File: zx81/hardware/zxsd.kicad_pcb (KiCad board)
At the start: 2 copper layers, 69.9 x 95.9 mm, 37 parts, among them J1 Micro_SD_Card, J2 ZX81_EXP, SW1 RESET, U1 74HCT32, U10 27C256, U11 KM62256CLP, U2 74HCT32, U3 74HCT00, U4 74HCT02, U5 74HCT163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

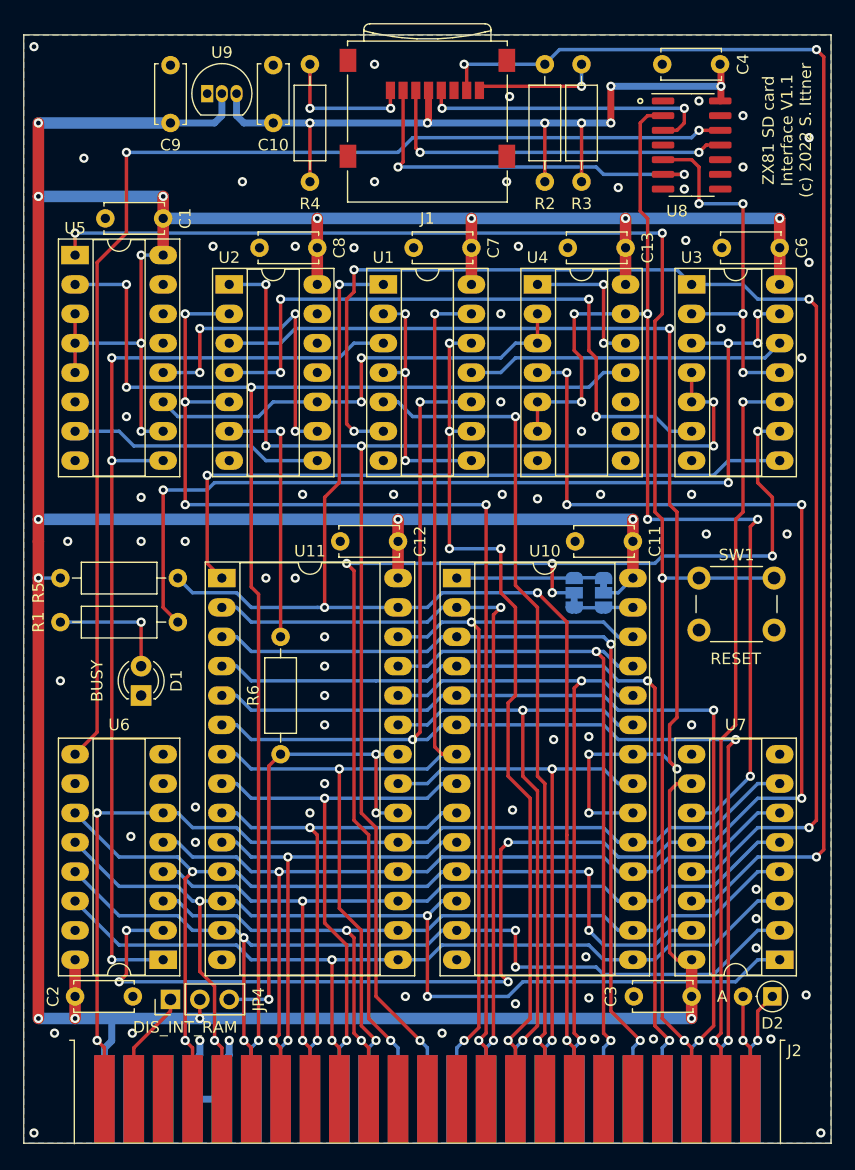
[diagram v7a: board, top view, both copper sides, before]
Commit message: fixed HRG issue, consider nRFSH for memory decoding
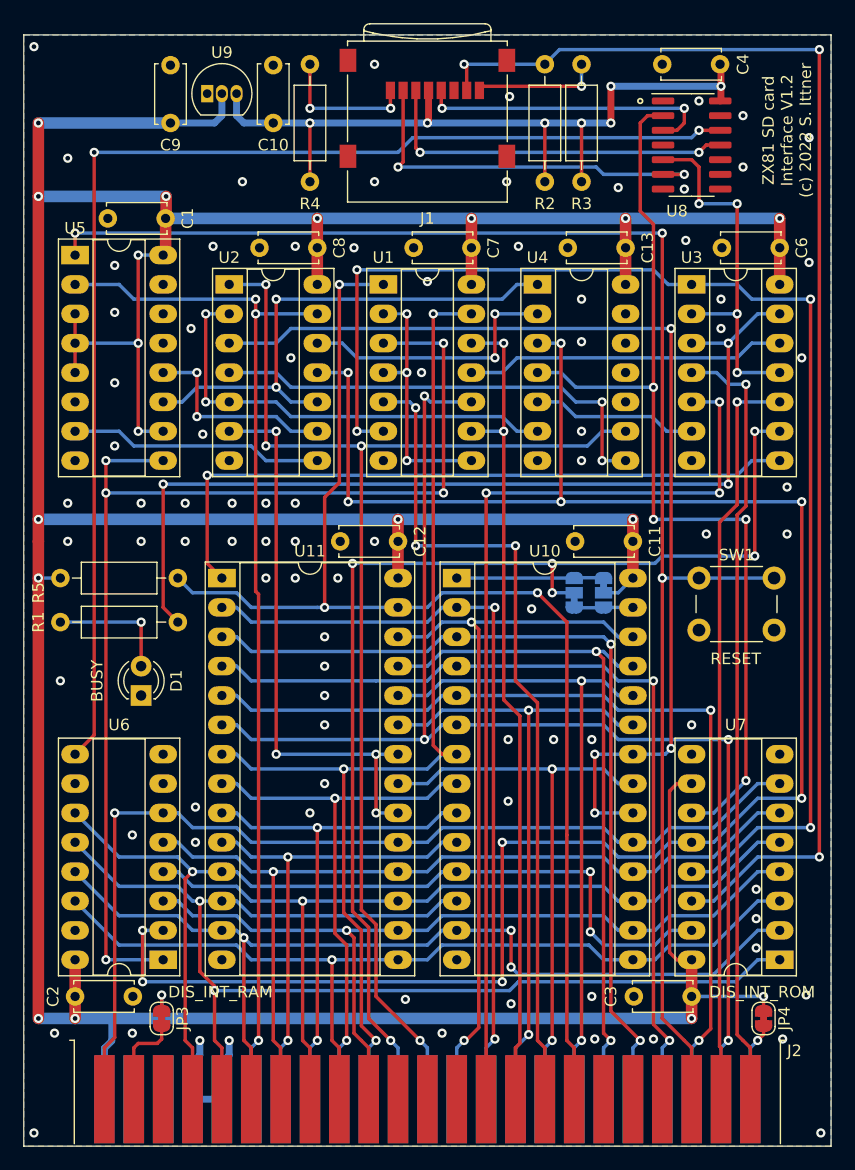
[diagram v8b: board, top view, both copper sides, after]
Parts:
- removed D2: BAT43, Diode_THT:D_DO-35_SOD27_P2.54mm_Vertical_AnodeUp
- removed R6: 680R, Resistor_THT:R_Axial_DIN0207_L6.3mm_D2.5mm_P10.16mm_Horizontal
- added JP3: DIS_INT_RAM, Jumper:SolderJumper-2_P1.3mm_Bridged_RoundedPad1.0x1.5mm, F.Cu at (124.3, 128.3)
- JP4: value DIS_INT_RAM -> DIS_INT_ROM; footprint Connector_PinHeader_2.54mm:PinHeader_1x03_P2.54mm_Vertical -> Jumper:SolderJumper-2_P1.3mm_Bridged_RoundedPad1.0x1.5mm
- U4: value 74HCT02 -> 74HCT04
- moved JP4 51.3 mm to (176.4, 128.3), turned to -90 degrees
- moved C1 0.21 mm to (124.7, 59.1)
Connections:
- JP4 pad 1: /nRAMCS_INT -> +5V
- JP4 pad 2: +5V -> /nROMCS_INT
- U2 pad 11: unconnected-(U2-Pad11) -> /nSD_CLK
- U2 pad 12: GND -> Net-(U2-Pad12)
- U2 pad 13: GND -> /CLK
- U2 pad 2: /nMREQ -> Net-(U2-Pad2)
- U2 pad 5: /nMREQ -> Net-(U2-Pad2)
- U2 pad 6: Net-(R6-Pad2) -> /nCS_RAM
- U3 pad 4: /A14 -> /nRFSH
- U3 pad 5: /A14 -> /nMREQ
- U3 pad 6: Net-(U2-Pad4) -> Net-(U3-Pad6)
- U4 pad 1: Net-(U4-Pad1) -> Net-(U2-Pad10)
- U4 pad 11: /CLK -> GND
- U4 pad 12: Net-(U4-Pad1) -> unconnected-(U4-Pad12)
- U4 pad 13: /SD_CLK -> GND
- U4 pad 2: Net-(U2-Pad10) -> Net-(U2-Pad12)
- U4 pad 3: Net-(U2-Pad10) -> /nSD_CLK
- U4 pad 4: /nSD_CLK -> /SD_CLK
- U4 pad 5: /SD_CLK -> Net-(U3-Pad6)
- U4 pad 6: /SD_CLK -> Net-(U2-Pad2)
- U4 pad 8: GND -> Net-(U2-Pad4)
- U4 pad 9: GND -> /A14
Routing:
- net /nRFSH: track 9.15 -> 67.8 mm
- net Net-(U2-Pad2): track 0.00 -> 39.4 mm, vias 0 -> 2
- net /nSD_CLK: track 141.8 -> 172.4 mm, vias 8 -> 10
- net /CLK: track 119.2 -> 91.1 mm, vias 4 -> 3
- net Net-(U2-Pad12): track 0.00 -> 23.4 mm, vias 0 -> 2
- net Net-(R6-Pad2): track 22.2 -> 0.00 mm, vias 1 -> 0
- net /nMREQ: track 102.1 -> 82.9 mm, vias 5 -> 3
- net Net-(U2-Pad4): track 56.7 -> 40.4 mm, vias 4 -> 2
- net /nSDWR: track 85.0 -> 100.5 mm, vias 3 -> 5
- net /A14: track 123.0 -> 107.7 mm, vias 6 -> 4
- net Net-(U3-Pad6): track 0.00 -> 14.4 mm
- net Net-(U4-Pad1): track 12.7 -> 0.00 mm, vias 2 -> 0
- net /SD_CLK: track 95.8 -> 84.0 mm, vias 6 -> 4
- net /D1: track 92.9 -> 104.1 mm, vias 4 -> 2
- net Net-(U2-Pad9): track 27.8 -> 17.7 mm, vias 4 -> 2
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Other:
- board size 69.9 x 95.9 mm -> 69.9 x 96.1 mm
- board text added: "DIS_INT_ROM"
- board text added: "ZX81 SD card Interface V1.2 (c) 2022 S. Ittner"
- board text removed: "ZX81 SD card Interface V1.1 (c) 2022 S. Ittner"
